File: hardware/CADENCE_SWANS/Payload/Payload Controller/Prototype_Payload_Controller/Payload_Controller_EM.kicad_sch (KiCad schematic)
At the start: 0 parts

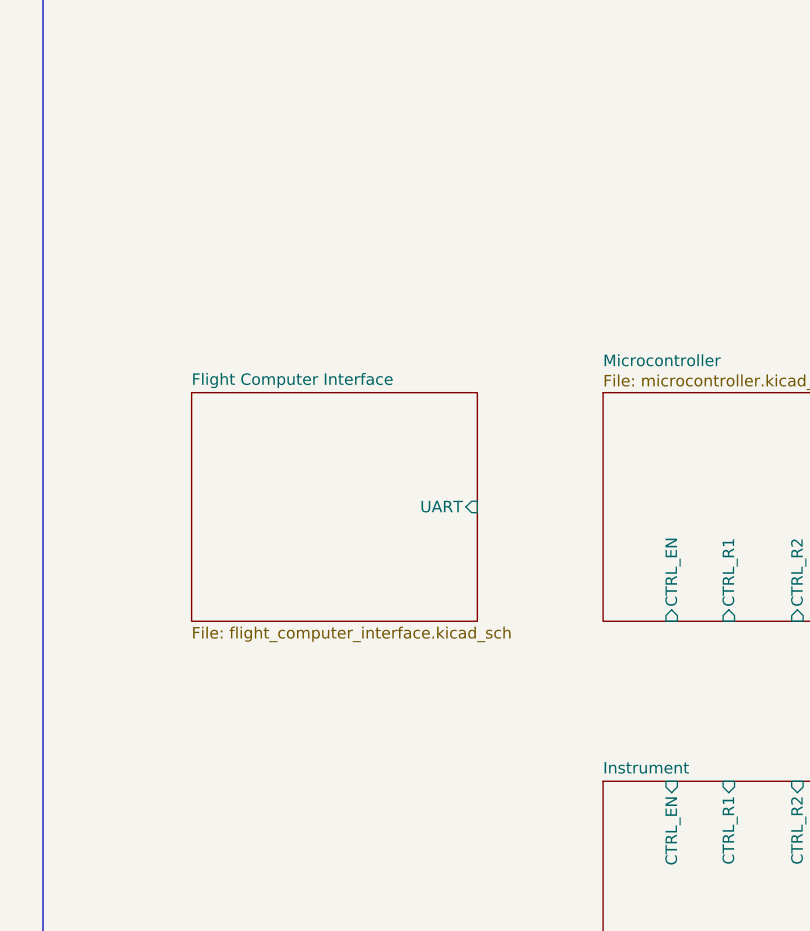
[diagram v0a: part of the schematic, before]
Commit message: added SN65C1668 symbol library and a folder for symbols
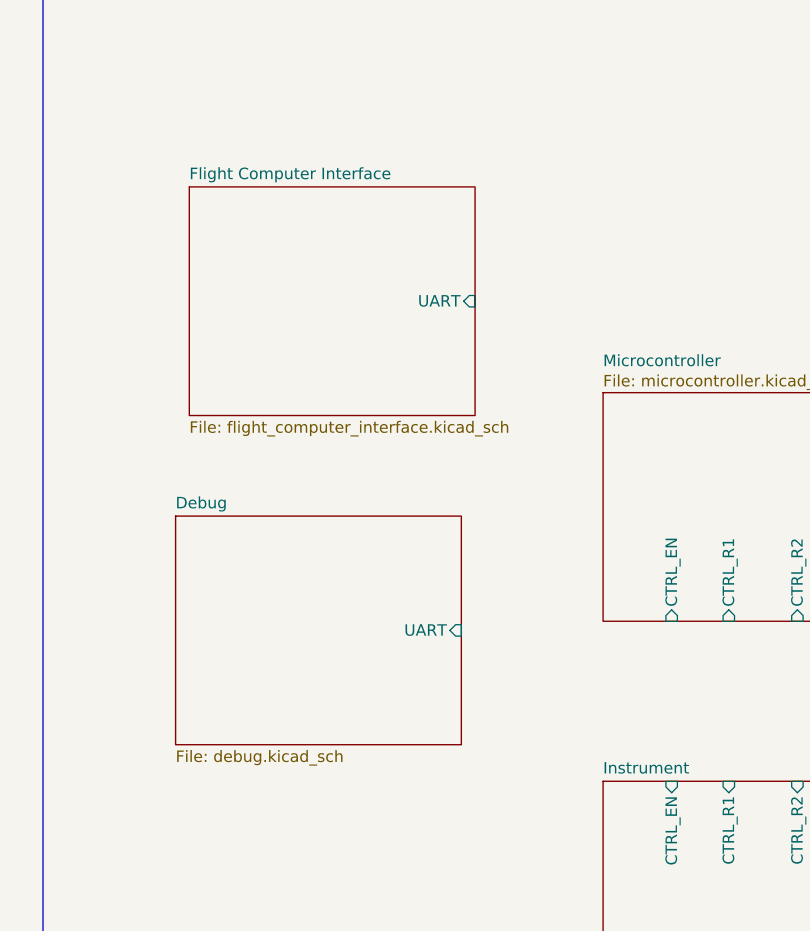
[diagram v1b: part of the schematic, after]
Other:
- added sheet Debug (debug.kicad_sch)
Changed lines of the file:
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@@
+	)
+	(sheet
+		(at 156.972 84.836)
+		(size 31.75 25.4)
+		(exclude_from_sim no)
+		(in_bom yes)
+		(on_board yes)
+		(dnp no)
+		(fields_autoplaced yes)
+		(stroke
+			(width 0.1524)
+			(type solid)
+		)
+		(fill
+			(color 0 0 0 0.0000)
+		)
+		(property "Sheetname" "Debug"
+			(at 156.972 84.1244 0)
+			(effects
+				(font
+					(size 1.27 1.27)
+				)
+				(justify left bottom)
+			)
+		)
+		(property "Sheetfile" "debug.kicad_sch"
+			(at 156.972 110.8206 0)
+			(effects
+				(font
+					(size 1.27 1.27)
+				)
+				(justify left top)
+			)
+		)
+		(pin "UART" input
+			(at 188.722 97.536 0)
+			(effects
+				(font
+					(size 1.27 1.27)
+				)
+				(justify right)
+			)
+		)
+		(instances
+			(project "Payload_Controller_EM"
+				(path "/866a965d-c307-40b7-9977-69e77fc0dc82"
+					(page "8")
+				)
+			)
+		)
 	)
 	(sheet
@@
 	)
 	(sheet
-		(at 158.75 71.12)
+		(at 158.496 48.26)
 		(size 31.75 25.4)
 		(exclude_from_sim no)
@@
 		)
 		(property "Sheetname" "Flight Computer Interface"
-			(at 158.75 70.4084 0)
+			(at 158.496 47.5484 0)
 			(effects
 				(font
@@
 		)
 		(property "Sheetfile" "flight_computer_interface.kicad_sch"
-			(at 158.75 97.1046 0)
+			(at 158.496 74.2446 0)
 			(effects
 				(font
@@
 		)
 		(pin "UART" input
-			(at 190.5 83.82 0)
-			(effects
-				(font
+			(at 190.246 60.96 0)
+			(effects
+				(font

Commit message: A whole lotta updates
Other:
- added sheet MRAM (mram.kicad_sch)
- sheet Flight Computer Interface: file flight_computer_interface.kicad_sch -> fc_interface.kicad_sch
- sheet Peripherals: file peripherals.kicad_sch -> perph.kicad_sch
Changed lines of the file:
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@@
 	)
 	(sheet
-		(at 156.972 84.836)
+		(at 156.972 96.266)
 		(size 31.75 25.4)
 		(exclude_from_sim no)
@@
 		)
 		(property "Sheetname" "Debug"
-			(at 156.972 84.1244 0)
+			(at 156.972 95.5544 0)
 			(effects
 				(font
@@
 		)
 		(property "Sheetfile" "debug.kicad_sch"
-			(at 156.972 110.8206 0)
+			(at 156.972 122.2506 0)
 			(effects
 				(font
@@
 		)
 		(pin "UART" input
-			(at 188.722 97.536 0)
+			(at 188.722 108.966 0)
 			(effects
 				(font
@@
 	(sheet
 		(at 254 71.12)
-		(size 27.94 24.13)
-		(exclude_from_sim no)
-		(in_bom yes)
-		(on_board yes)
-		(dnp no)
-		(fields_autoplaced yes)
-		(stroke
-			(width 0.1524)
-			(type solid)
-		)
-		(fill
-			(color 0 0 0 0.0000)
-		)
-		(property "Sheetname" "Peripherals"
+		(size 27.94 22.86)
+		(exclude_from_sim no)
+		(in_bom yes)
+		(on_board yes)
+		(dnp no)
+		(fields_autoplaced yes)
+		(stroke
+			(width 0.1524)
+			(type solid)
+		)
+		(fill
+			(color 0 0 0 0.0000)
+		)
+		(property "Sheetname" "MRAM"
 			(at 254 70.4084 0)
 			(effects
@@
 			)
 		)
-		(property "Sheetfile" "peripherals.kicad_sch"
-			(at 254 95.8346 0)
-			(effects
-				(font
-					(size 1.27 1.27)
-				)
-				(justify left top)
+		(property "Sheetfile" "mram.kicad_sch"
+			(at 254 94.5646 0)
+			(effects
+				(font
+					(size 1.27 1.27)
+				)
+				(justify left top)
+			)
+		)
+		(pin "MRAM_ADDRESS" input
+			(at 254 82.55 180)
+			(effects
+				(font
+					(size 1.27 1.27)
+				)
+				(justify left)
+			)
+		)
+		(pin "MRAM_CTRL" input
+			(at 254 77.47 180)
+			(effects
+				(font
+					(size 1.27 1.27)
+				)
+				(justify left)
+			)
+		)
+		(pin "MRAM_DATA" input
+			(at 254 87.63 180)
+			(effects
+				(font
+					(size 1.27 1.27)
+				)
+				(justify left)
 			)
 		)
@@
 	)
 	(sheet
-		(at 158.496 48.26)
-		(size 31.75 25.4)
+		(at 160.02 44.45)
+		(size 18.796 12.7)
 		(exclude_from_sim no)
 		(in_bom yes)
@@
 		)
 		(property "Sheetname" "Flight Computer Interface"
-			(at 158.496 47.5484 0)
-			(effects
-				(font
-					(size 1.27 1.27)
-				)
-				(justify left bottom)
-			)
-		)
-		(property "Sheetfile" "flight_computer_interface.kicad_sch"
-			(at 158.496 74.2446 0)
+			(at 160.02 43.7384 0)
+			(effects
+				(font
+					(size 1.27 1.27)
+				)
+				(justify left bottom)
+			)
+		)
+		(property "Sheetfile" "fc_interface.kicad_sch"
+			(at 160.02 57.7346 0)
 			(effects
 				(font
@@
 		)
 		(pin "UART" input
-			(at 190.246 60.96 0)
+			(at 178.816 50.8 0)
 			(effects
 				(font
@@
 				)
 			)
+		)
+	)
+	(sheet
+		(at 210.82 49.53)
+		(size 20.32 12.7)
+		(exclude_from_sim no)
+		(in_bom yes)
+		(on_board yes)
+		(dnp no)
+		(fields_autoplaced yes)
+		(stroke
+			(width 0.1524)
+			(type solid)
+		)
+		(fill
+			(color 0 0 0 0.0000)
+		)
+		(property "Sheetname" "Peripherals"
+			(at 210.82 48.8184 0)
+			(effects
+				(font
+					(size 1.27 1.27)
+				)
+				(justify left bottom)
+			)
+		)
+		(property "Sheetfile" "perph.kicad_sch"
+			(at 210.82 62.8146 0)
+			(effects
+				(font
+					(size 1.27 1.27)
+				)
+				(justify left top)
+			)
+		)
+		(instances
+			(project "Payload_Controller_EM"
+				(path "/866a965d-c307-40b7-9977-69e77fc0dc82"
+					(page "9")
+				)
+			)

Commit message: updates
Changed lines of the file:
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@@
+		)
+	)
+	(wire
+		(pts
+			(xy 107.95 82.55) (xy 113.03 82.55)
+		)
+		(stroke
+			(width 0)
+			(type default)
+		)
+	)
+	(wire
+		(pts
+			(xy 60.96 86.36) (xy 77.47 86.36)
+		)
+		(stroke
+			(width 0)
+			(type default)
+		)
+	)
+	(symbol
+		(lib_id "power:+3V3")
+		(at 113.03 82.55 0)
+		(unit 1)
+		(exclude_from_sim no)
+		(in_bom yes)
+		(on_board yes)
+		(dnp no)
+		(fields_autoplaced yes)
+		(property "Reference" "#PWR05"
+			(at 113.03 86.36 0)
+			(effects
+				(font
+					(size 1.27 1.27)
+				)
+				(hide yes)
+			)
+		)
+		(property "Value" "+3V3"
+			(at 113.03 77.47 0)
+			(effects
+				(font
+					(size 1.27 1.27)
+				)
+			)
+		)
+		(property "Footprint" ""
+			(at 113.03 82.55 0)
+			(effects
+				(font
+					(size 1.27 1.27)
+				)
+				(hide yes)
+			)
+		)
+		(property "Datasheet" ""
+			(at 113.03 82.55 0)
+			(effects
+				(font
+					(size 1.27 1.27)
+				)
+				(hide yes)
+			)
+		)
+		(property "Description" "Power symbol creates a global label with name \"+3V3\""
+			(at 113.03 82.55 0)
+			(effects
+				(font
+					(size 1.27 1.27)
+				)
+				(hide yes)
+			)
+		)
+		(pin "1"
+		)
+		(instances
+			(project ""
+				(path "/866a965d-c307-40b7-9977-69e77fc0dc82"
+					(reference "#PWR05")
+					(unit 1)
+				)
+			)
 		)
 	)

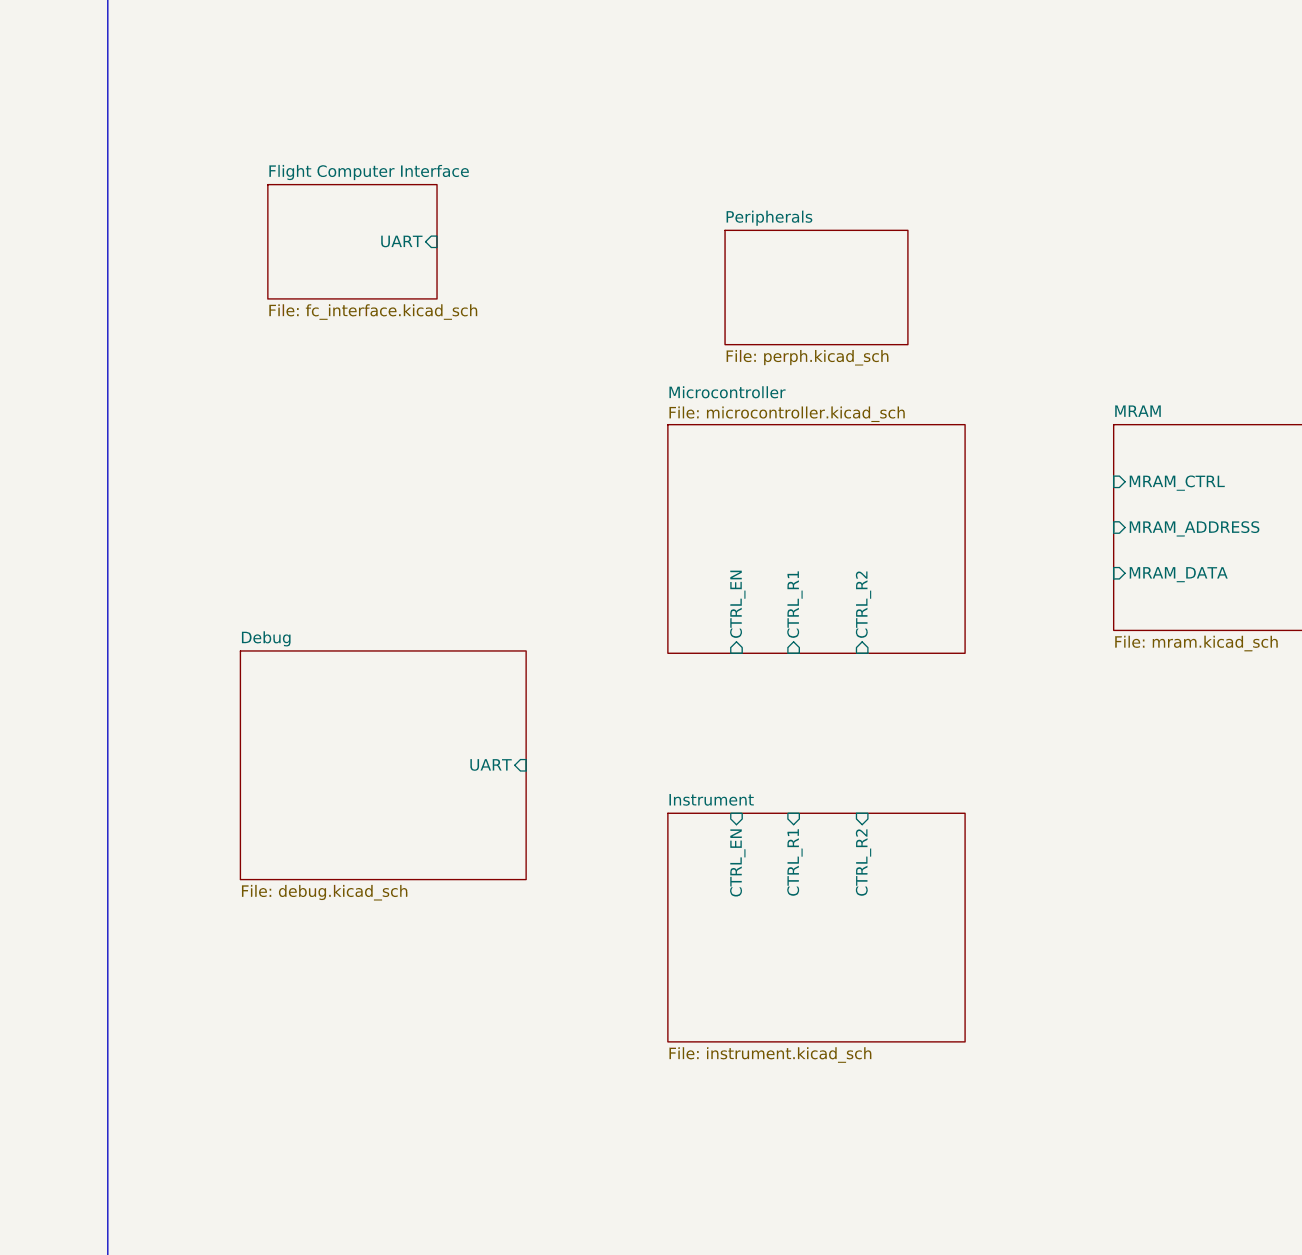
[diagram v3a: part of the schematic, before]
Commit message: updated MRAM Schematic Symbol
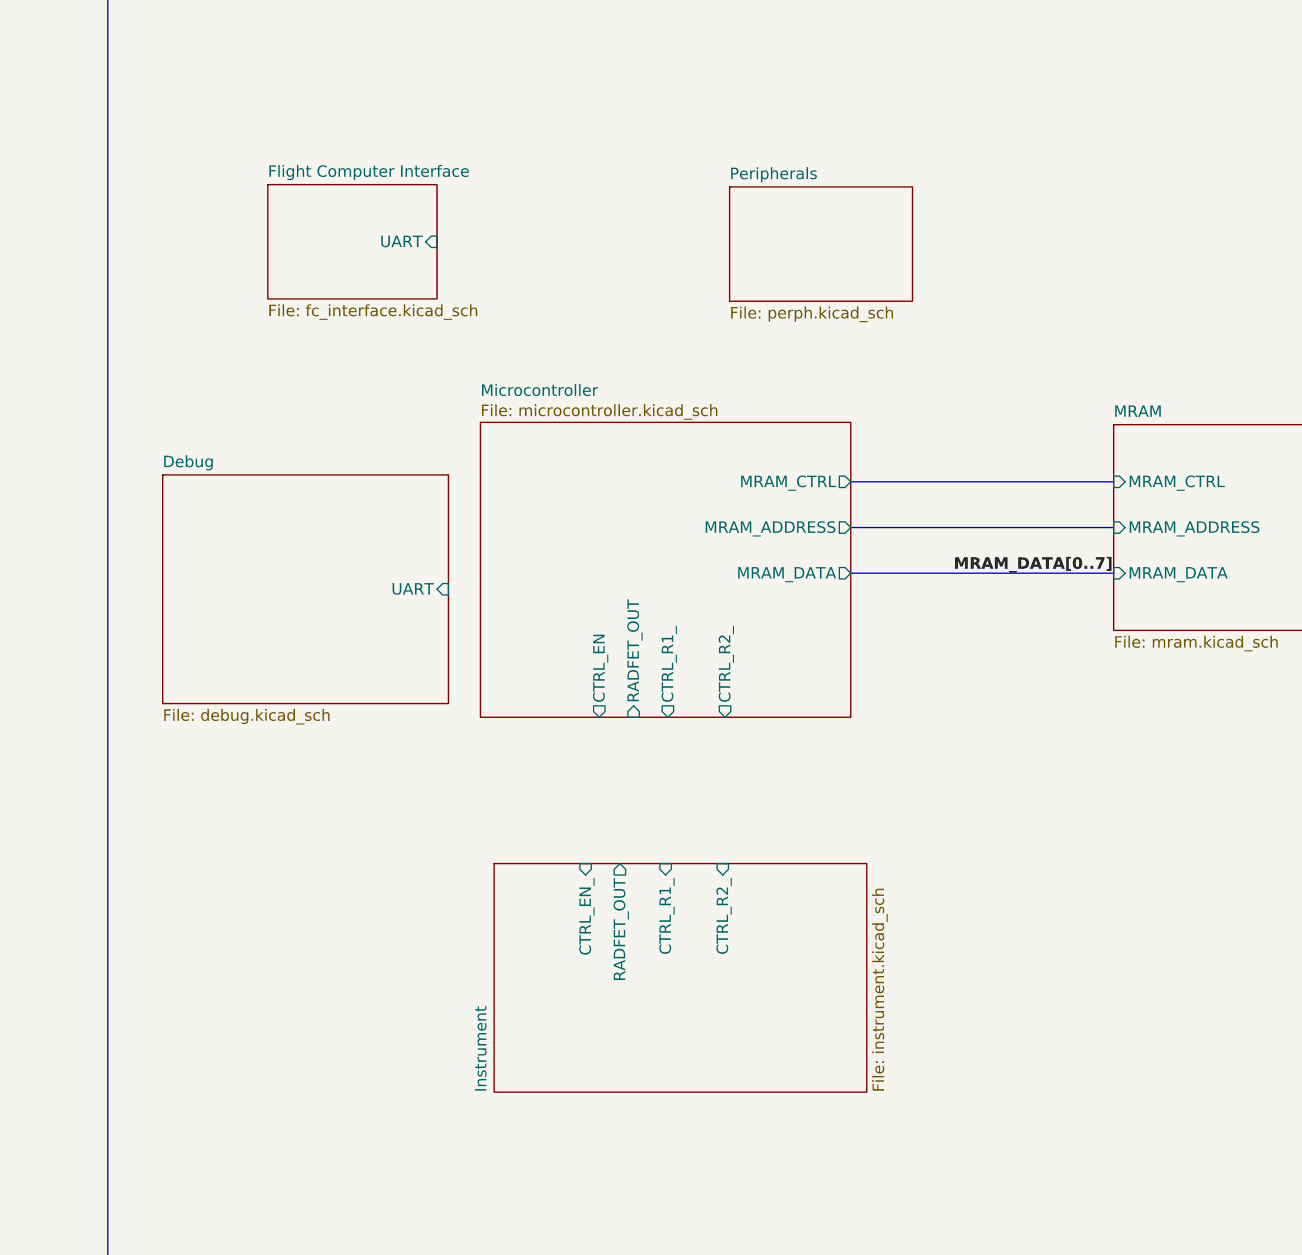
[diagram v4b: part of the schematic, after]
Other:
- sheet Instrument ports: added CTRL_EN_, CTRL_R1_, CTRL_R2_, RADFET_OUT; removed CTRL_EN, CTRL_R1, CTRL_R2
- sheet Microcontroller ports: added CTRL_R1_, CTRL_R2_, MRAM_ADDRESS, MRAM_CTRL, MRAM_DATA, RADFET_OUT; removed CTRL_R1, CTRL_R2
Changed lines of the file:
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@@
+	(bus
+		(pts
+			(xy 224.79 77.47) (xy 254 77.47)
+		)
+		(stroke
+			(width 0)
+			(type default)
+		)
+	)
+	(bus
+		(pts
+			(xy 224.79 87.63) (xy 254 87.63)
+		)
+		(stroke
+			(width 0)
+			(type default)
+		)
+	)
 	(bus
 		(pts
@@
 		)
 	)
+	(bus
+		(pts
+			(xy 224.79 82.55) (xy 254 82.55)
+		)
+		(stroke
+			(width 0)
+			(type default)
+		)
+	)
 	(wire
 		(pts
@@
 			(width 0)
 			(type default)
+		)
+	)
+	(label "MRAM_DATA[0..7]"
+		(at 236.22 87.63 0)
+		(effects
+			(font
+				(size 1.27 1.27)
+				(thickness 0.254)
+				(bold yes)
+			)
+			(justify left bottom)
 		)
 	)
@@
 	)
 	(sheet
-		(at 156.972 96.266)
+		(at 148.336 76.708)
 		(size 31.75 25.4)
 		(exclude_from_sim no)
@@
 		)
 		(property "Sheetname" "Debug"
-			(at 156.972 95.5544 0)
+			(at 148.336 75.9964 0)
 			(effects
 				(font
@@
 		)
 		(property "Sheetfile" "debug.kicad_sch"
-			(at 156.972 122.2506 0)
+			(at 148.336 102.6926 0)
 			(effects
 				(font
@@
 		)
 		(pin "UART" input
-			(at 188.722 108.966 0)
+			(at 180.086 89.408 0)
 			(effects
 				(font
@@
 	)
 	(sheet
-		(at 204.47 71.12)
-		(size 33.02 25.4)
+		(at 183.642 70.866)
+		(size 41.148 32.766)
 		(exclude_from_sim no)
 		(in_bom yes)
@@
 		)
 		(property "Sheetname" "Microcontroller"
-			(at 204.47 68.326 0)
+			(at 183.642 68.072 0)
 			(effects
 				(font
@@
 		)
 		(property "Sheetfile" "microcontroller.kicad_sch"
-			(at 204.47 69.088 0)
-			(effects
-				(font
-					(size 1.27 1.27)
-				)
-				(justify left top)
-			)
-		)
-		(pin "CTRL_EN" input
-			(at 212.09 96.52 270)
-			(effects
-				(font
-					(size 1.27 1.27)
-				)
-				(justify left)
-			)
-		)
-		(pin "CTRL_R1" input
-			(at 218.44 96.52 270)
-			(effects
-				(font
-					(size 1.27 1.27)
-				)
-				(justify left)
-			)
-		)
-		(pin "CTRL_R2" input
-			(at 226.06 96.52 270)
-			(effects
-				(font
-					(size 1.27 1.27)
-				)
-				(justify left)
+			(at 183.642 68.834 0)
+			(effects
+				(font
+					(size 1.27 1.27)
+				)
+				(justify left top)
+			)
+		)
+		(pin "CTRL_EN" output
+			(at 196.85 103.632 270)
+			(effects
+				(font
+					(size 1.27 1.27)
+				)
+				(justify left)
+			)
+		)
+		(pin "CTRL_R1_" output
+			(at 204.47 103.632 270)
+			(effects
+				(font
+					(size 1.27 1.27)
+				)
+				(justify left)
+			)
+		)
+		(pin "CTRL_R2_" output
+			(at 210.82 103.632 270)
+			(effects
+				(font
+					(size 1.27 1.27)
+				)
+				(justify left)
+			)
+		)
+		(pin "RADFET_OUT" input
+			(at 200.66 103.632 270)
+			(effects
+				(font
+					(size 1.27 1.27)
+				)
+				(justify left)
+			)
+		)
+		(pin "MRAM_CTRL" output
+			(at 224.79 77.47 0)
+			(effects
+				(font
+					(size 1.27 1.27)
+				)
+				(justify right)
+			)
+		)
+		(pin "MRAM_DATA" output
+			(at 224.79 87.63 0)
+			(effects
+				(font
+					(size 1.27 1.27)
+				)
+				(justify right)
+			)
+		)
+		(pin "MRAM_ADDRESS" output
+			(at 224.79 82.55 0)
+			(effects
+				(font
+					(size 1.27 1.27)
+				)
+				(justify right)
 			)
 		)
@@
 	)
 	(sheet
-		(at 210.82 49.53)
+		(at 211.328 44.704)
 		(size 20.32 12.7)
 		(exclude_from_sim no)
@@
 		)
 		(property "Sheetname" "Peripherals"
-			(at 210.82 48.8184 0)
+			(at 211.328 43.9924 0)
 			(effects
 				(font
@@
 		)
 		(property "Sheetfile" "perph.kicad_sch"
-			(at 210.82 62.8146 0)
+			(at 211.328 57.9886 0)
 			(effects
 				(font
@@
 	)
 	(sheet
-		(at 204.47 114.3)
-		(size 33.02 25.4)
+		(at 185.166 119.888)
+		(size 41.402 25.4)
 		(exclude_from_sim no)
 		(in_bom yes)
@@
 		)
 		(property "Sheetname" "Instrument"
-			(at 204.47 113.5884 0)
+			(at 184.4544 145.288 90)
 			(effects
 				(font
@@
 		)
 		(property "Sheetfile" "instrument.kicad_sch"
-			(at 204.47 140.2846 0)
-			(effects
-				(font
-					(size 1.27 1.27)
-				)
-				(justify left top)
-			)
-		)
-		(pin "CTRL_EN" input
-			(at 212.09 114.3 90)
-			(effects
-				(font
-					(size 1.27 1.27)
-				)
-				(justify right)
-			)
-		)
-		(pin "CTRL_R1" input
-			(at 218.44 114.3 90)
-			(effects
-				(font
-					(size 1.27 1.27)
-				)
-				(justify right)
-			)
-		)
-		(pin "CTRL_R2" input
-			(at 226.06 114.3 90)
-			(effects
-				(font
+			(at 227.1526 145.288 90)
+			(effects
+				(font
+					(size 1.27 1.27)
+				)
+				(justify left top)
+			)
+		)
+		(pin "CTRL_R2_" input
+			(at 210.566 119.888 90)
+			(effects
+				(font
+					(size 1.27 1.27)
+				)
+				(justify right)
+			)
+		)
+		(pin "CTRL_R1_" input
+			(at 204.216 119.888 90)
+			(effects
+				(font
+					(size 1.27 1.27)
+				)
+				(justify right)
+			)
+		)
+		(pin "CTRL_EN_" input
+			(at 195.326 119.888 90)
+			(effects
+				(font
+					(size 1.27 1.27)
+				)
+				(justify right)
+			)
+		)
+		(pin "RADFET_OUT" output
+			(at 199.136 119.888 90)
+			(effects
+				(font
